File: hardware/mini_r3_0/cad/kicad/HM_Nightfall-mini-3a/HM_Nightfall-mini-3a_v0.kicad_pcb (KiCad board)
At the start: 2 copper layers, 39 x 70 mm, 97 parts, among them J2 FAN_2S3S, K1 62201021121, P1 BATTERY, Q2 IRLML6402TRPBF, Q3 IRLML6344TRPBF, U1 AP2210N-3.3TRG1, U2 MP6551GQB-P, U3 MP6551GQB-P, U4 ISM330DHCXTR, U5 STM32F413CHU6TRUFQFPN-48_7X7X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, U6 CY15B108QI-20LPXC, U7 MPM3610GQV-P

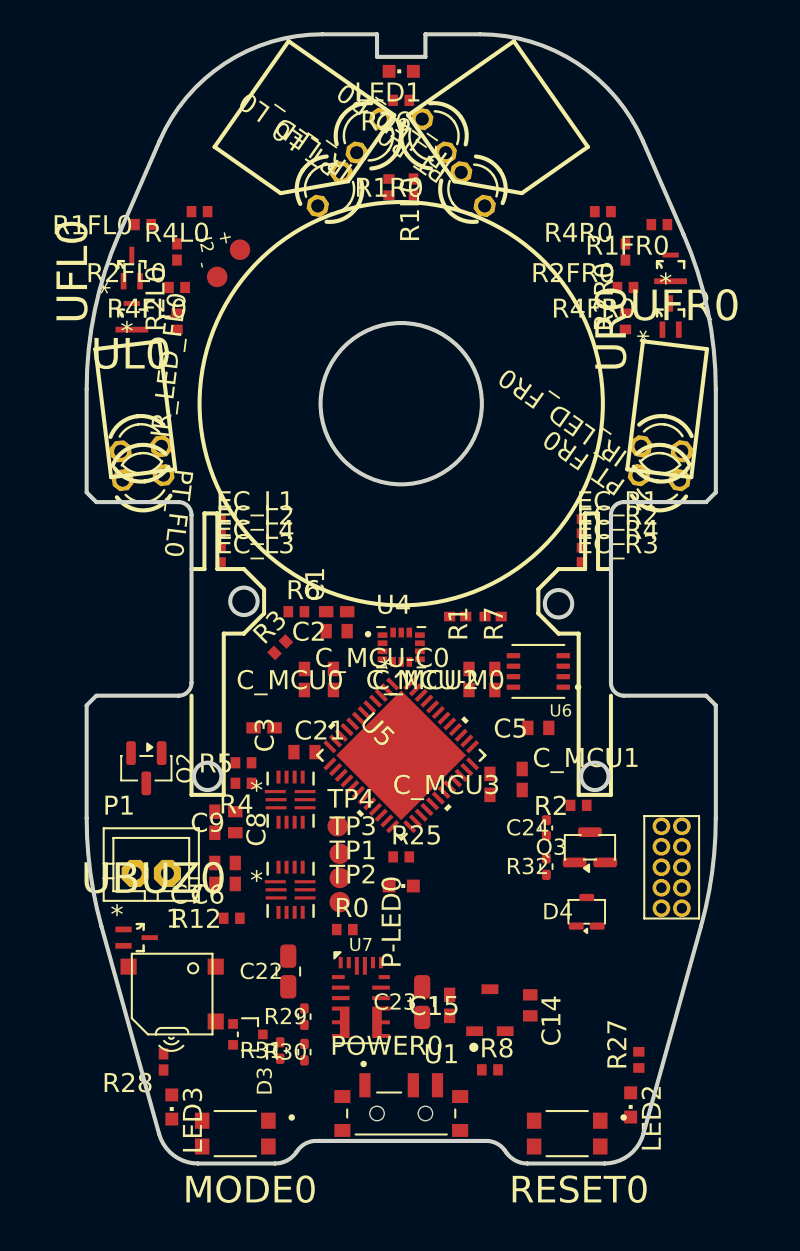
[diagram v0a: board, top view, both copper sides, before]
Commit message: Checkpoint mini_r3 four-layer routing
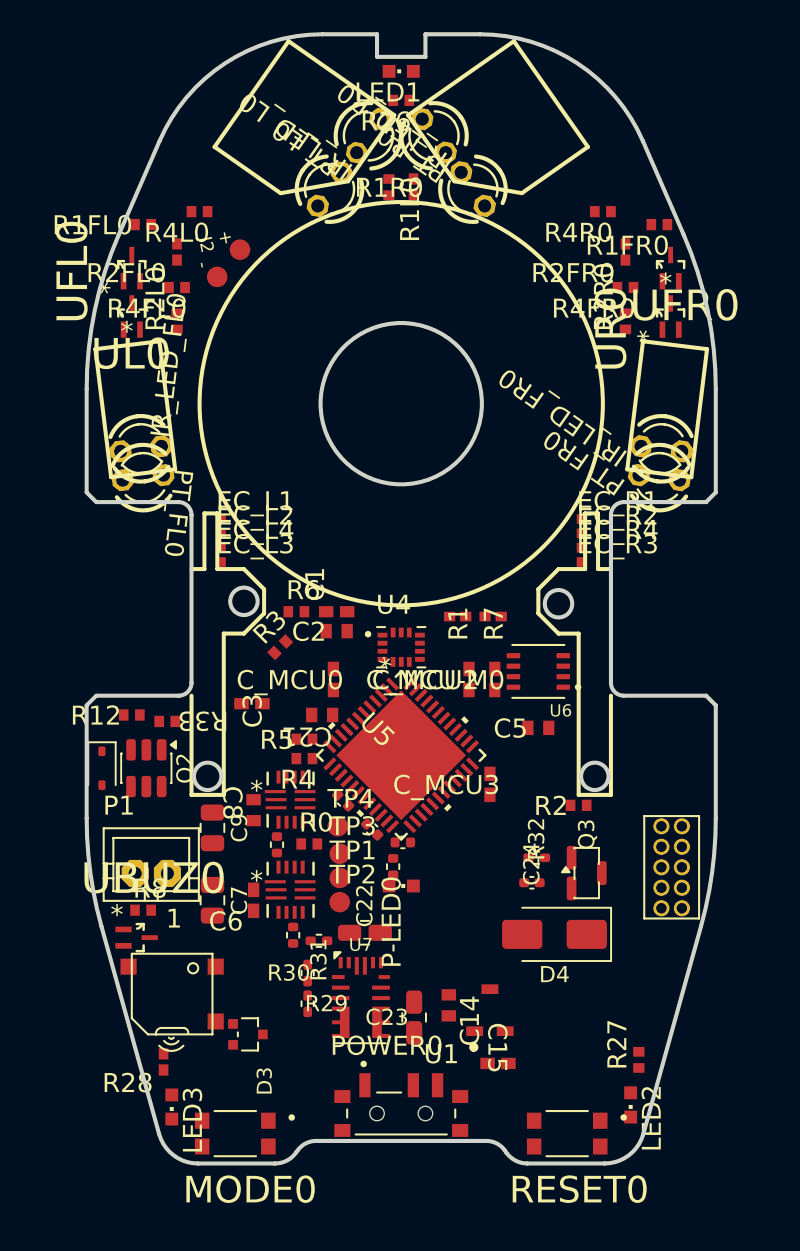
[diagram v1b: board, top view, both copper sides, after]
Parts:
- added C25: 100nF X7R, Capacitor_SMD:C_0402_1005Metric, F.Cu at (144.9, 117.5)
- added D5: BZT52-C15S_R1_00001, Diode_SMD:D_SOD-323, F.Cu at (129.9, 115.5)
- added R33: 4.7k, HM_Nightfall-mini-2e_v1:R0402, F.Cu at (134.0, 112.6)
- added R34: 220k, Resistor_SMD:R_0402_1005Metric, F.Cu at (141.8, 125.8)
- added R35: 220k, Resistor_SMD:R_0402_1005Metric, F.Cu at (140.8, 120.2)
- C7, C9: footprint HM_Nightfall-mini-2e_v1:C0402 -> Capacitor_SMD:C_0805_2012Metric
- C_MCU-C0, C_MCU1: footprint HM_Nightfall-mini-2e_v1:C0402 -> Capacitor_SMD:C_0402_1005Metric
- D4: value BAS16WT1GW -> SM340A; footprint Package_TO_SOT_SMD:SOT-323_SC-70 -> Diode_SMD:D_SMA
- Q2: value IRLML6402TRPBF -> PJS6403_S1_00001; footprint Package_TO_SOT_SMD:SOT-23 -> Package_TO_SOT_SMD:SOT-23-6
- R25: footprint HM_Nightfall-mini-2e_v1:R0402 -> Resistor_SMD:R_0402_1005Metric
- moved R8 23.7 mm to (132.5, 124.3)
- moved R12 14.0 mm to (131.8, 112.2)
- moved C_MCU-C0 10.2 mm to (146.7, 119.3), turned to -45 degrees
- moved C_MCU1 8.36 mm to (148.6, 120.1), turned to 180 degrees
- moved R31 7.21 mm to (143.4, 126.2), turned to 180 degrees
- moved R0 5.74 mm to (142.8, 120.2)
- moved C22 5.32 mm to (146.2, 125.7), turned to 0 degrees
- moved C14 5.05 mm to (151.4, 130.2)
- moved R30 4.90 mm to (142.7, 128.2)
- moved C15 4.69 mm to (154.5, 133.8), turned to 180 degrees
- moved R4 4.08 mm to (142.5, 114.9)
- moved R5 4.05 mm to (142.5, 113.7)
- moved C24 3.52 mm to (156.6, 122.6), turned to 0 degrees
- moved C21 2.55 mm to (143.6, 112.2), turned to 180 degrees
- moved D4 2.44 mm to (158.0, 125.8), turned to 180 degrees
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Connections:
- D4 pad 2: (no net) -> VBAT_SW
- LED2 pad C: GND2 -> GND
- LED3 pad C: GND2 -> GND
- MODE0 pad 3: GND2 -> GND
- MODE0 pad 4: GND2 -> GND
- POWER0 pad 2: /PWR_GATE_INTERNAL -> /PWR_SWITCH_RETURN
- Q2 pad 1: /PWR_GATE_INTERNAL -> VBAT_SW
- Q2 pad 2: VBAT_RAW -> VBAT_SW
- Q2 pad 3: VBAT_SW -> /PWR_GATE_INTERNAL
- R5 pad 1: GND2 -> GND
- RESET0 pad 3: GND2 -> GND
- RESET0 pad 4: GND2 -> GND
- U2 pad 6: GND2 -> /MOTOR_R_SR
- U3 pad 6: GND2 -> /MOTOR_L_SR
- U7 pad 4: unconnected-(U7-SW-Pad4) -> /MPM_SW_INTERNAL
- U7 pad 5: unconnected-(U7-SW-Pad4) -> /MPM_SW_INTERNAL
- U7 pad 6: unconnected-(U7-SW-Pad4) -> /MPM_SW_INTERNAL
